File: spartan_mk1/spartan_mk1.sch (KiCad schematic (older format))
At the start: 0 parts

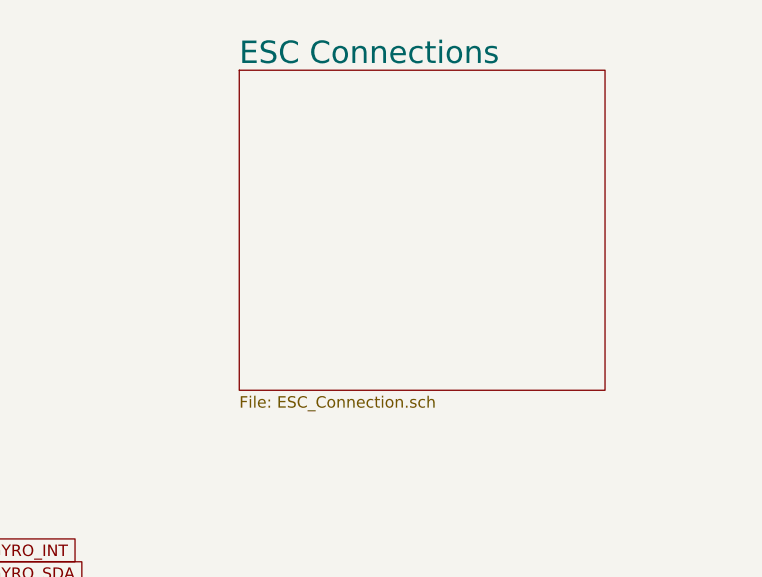
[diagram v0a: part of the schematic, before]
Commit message: Added ESC connectors in schematic
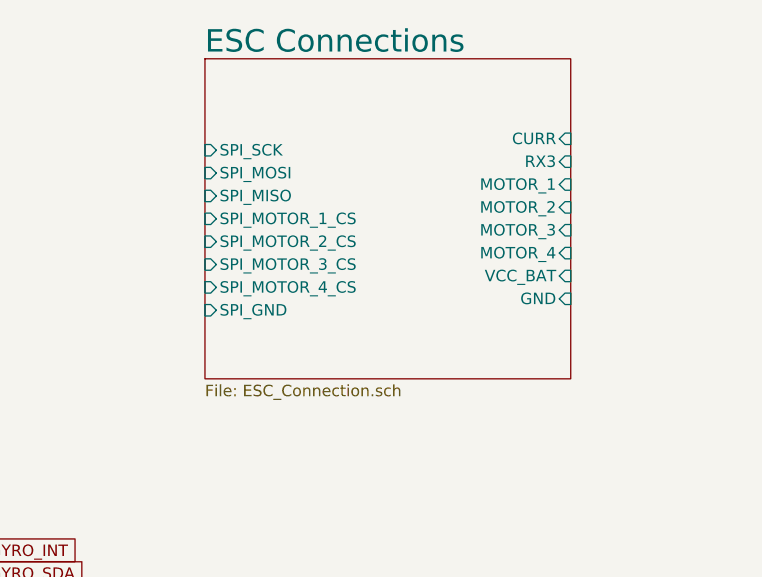
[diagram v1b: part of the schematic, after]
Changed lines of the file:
@@
 	7650 4150 7600 4150
 $Sheet
-S 8800 1450 1600 1400
+S 8650 1400 1600 1400
 U 5FB6E842
 F0 "ESC Connections" 98
 F1 "ESC_Connection.sch" 50
+F2 "GND" I R 10250 2450 50
+F3 "VCC_BAT" I R 10250 2350 50
+F4 "MOTOR_1" I R 10250 1950 50
+F5 "MOTOR_2" I R 10250 2050 50
+F6 "MOTOR_3" I R 10250 2150 50
+F7 "MOTOR_4" I R 10250 2250 50
+F8 "RX3" I R 10250 1850 50
+F9 "CURR" I R 10250 1750 50
+F10 "SPI_SCK" I L 8650 1800 50
+F11 "SPI_MOSI" I L 8650 1900 50
+F12 "SPI_MISO" I L 8650 2000 50
+F13 "SPI_MOTOR_1_CS" I L 8650 2100 50
+F14 "SPI_MOTOR_2_CS" I L 8650 2200 50
+F15 "SPI_MOTOR_3_CS" I L 8650 2300 50
+F16 "SPI_MOTOR_4_CS" I L 8650 2400 50
+F17 "SPI_GND" I L 8650 2500 50
 $EndSheet
 $Sheet

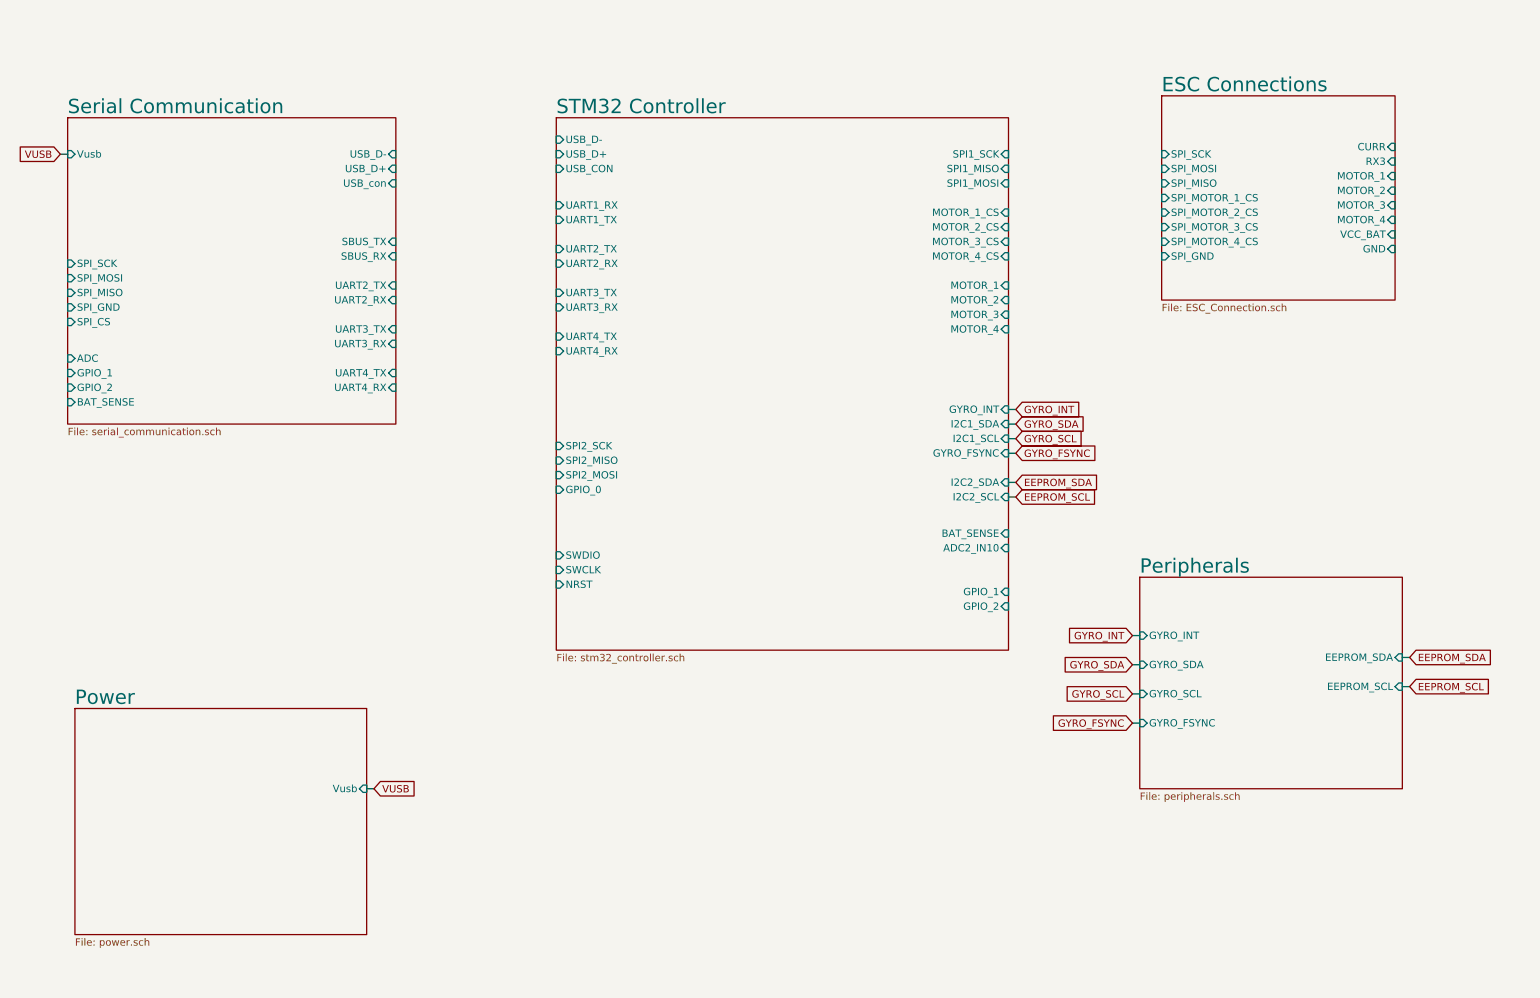
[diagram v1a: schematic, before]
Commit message: Complete schematic with DRC done
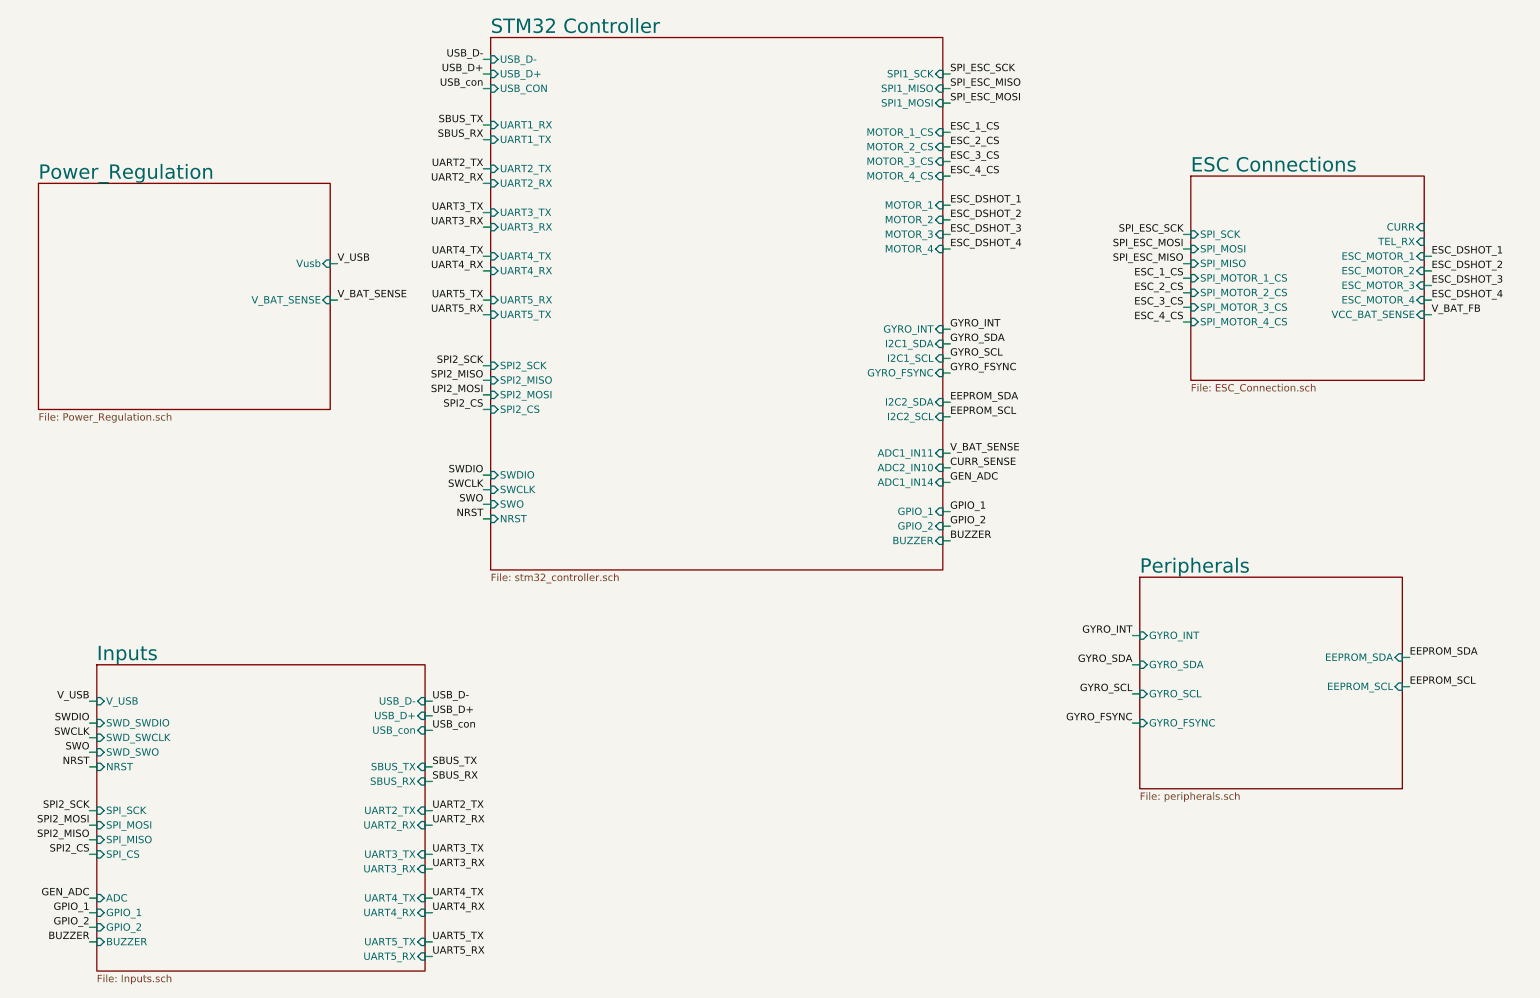
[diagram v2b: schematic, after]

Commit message: updated placement
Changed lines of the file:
@@
 Wire Wire Line
 	1300 5700 1350 5700
+Text Label 10500 2300 0    50   ~ 0
+CURR_SENSE
+Wire Wire Line
+	10500 2300 10450 2300
+Text Label 10500 2400 0    50   ~ 0
+UART3_RX
+Wire Wire Line
+	10500 2400 10450 2400
 $EndSCHEMATC

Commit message: Routing in progress
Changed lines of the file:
@@
 F7 "EEPROM_SCL" I R 10300 5450 50
 $EndSheet
-$Sheet
-S 1350 5300 2250 2100
-U 5F78701C
-F0 "Inputs" 98
-F1 "Inputs.sch" 50
-F2 "USB_D-" I R 3600 5550 50
-F3 "USB_D+" I R 3600 5650 50
-F4 "UART2_TX" I R 3600 6300 50
-F5 "UART2_RX" I R 3600 6400 50
-F6 "UART3_TX" I R 3600 6600 50
-F7 "UART3_RX" I R 3600 6700 50
-F8 "UART4_TX" I R 3600 6900 50
-F9 "UART4_RX" I R 3600 7000 50
-F10 "SPI_SCK" I L 1350 6300 50
-F11 "SPI_MOSI" I L 1350 6400 50
-F12 "SPI_MISO" I L 1350 6500 50
-F13 "SPI_CS" I L 1350 6600 50
-F14 "USB_con" I R 3600 5750 50
-F15 "GPIO_1" I L 1350 7000 50
-F16 "GPIO_2" I L 1350 7100 50
-F17 "ADC" I L 1350 6900 50
-F18 "SBUS_RX" I R 3600 6100 50
-F19 "SBUS_TX" I R 3600 6000 50
-F20 "UART5_TX" I R 3600 7200 50
-F21 "UART5_RX" I R 3600 7300 50
-F22 "V_USB" I L 1350 5550 50
-F23 "SWD_SWDIO" I L 1350 5700 50
-F24 "SWD_SWCLK" I L 1350 5800 50
-F25 "SWD_SWO" I L 1350 5900 50
-F26 "NRST" I L 1350 6000 50
-F27 "BUZZER" I L 1350 7200 50
-$EndSheet
 Wire Wire Line
 	8450 5100 8500 5100
@@
 Wire Wire Line
 	7200 3600 7150 3600
-$Sheet
-S 4050 1000 3100 3650
-U 5F6A010E
-F0 "STM32 Controller" 98
-F1 "stm32_controller.sch" 50
-F2 "USB_D-" I L 4050 1150 50
-F3 "USB_D+" I L 4050 1250 50
-F4 "UART1_RX" I L 4050 1600 50
-F5 "UART1_TX" I L 4050 1700 50
-F6 "UART2_TX" I L 4050 1900 50
-F7 "UART2_RX" I L 4050 2000 50
-F8 "UART3_TX" I L 4050 2200 50
-F9 "UART3_RX" I L 4050 2300 50
-F10 "UART4_TX" I L 4050 2500 50
-F11 "UART4_RX" I L 4050 2600 50
-F12 "I2C1_SDA" I R 7150 3100 50
-F13 "I2C1_SCL" I R 7150 3200 50
-F14 "I2C2_SCL" I R 7150 3600 50
-F15 "I2C2_SDA" I R 7150 3500 50
-F16 "SPI1_SCK" I R 7150 1250 50
-F17 "SPI1_MISO" I R 7150 1350 50
-F18 "SPI1_MOSI" I R 7150 1450 50
-F19 "SPI2_SCK" I L 4050 3250 50
-F20 "SPI2_MISO" I L 4050 3350 50
-F21 "SPI2_MOSI" I L 4050 3450 50
-F22 "MOTOR_4" I R 7150 2450 50
-F23 "MOTOR_3" I R 7150 2350 50
-F24 "MOTOR_2" I R 7150 2250 50
-F25 "MOTOR_1" I R 7150 2150 50
-F26 "GYRO_FSYNC" I R 7150 3300 50
-F27 "GYRO_INT" I R 7150 3000 50
-F28 "MOTOR_1_CS" I R 7150 1650 50
-F29 "MOTOR_2_CS" I R 7150 1750 50
-F30 "MOTOR_3_CS" I R 7150 1850 50
-F31 "MOTOR_4_CS" I R 7150 1950 50
-F32 "ADC2_IN10" I R 7150 3950 50
-F33 "GPIO_1" I R 7150 4250 50
-F34 "SWDIO" I L 4050 4000 50
-F35 "SWCLK" I L 4050 4100 50
-F36 "NRST" I L 4050 4300 50
-F37 "GPIO_2" I R 7150 4350 50
-F38 "USB_CON" I L 4050 1350 50
-F39 "UART5_RX" I L 4050 2800 50
-F40 "UART5_TX" I L 4050 2900 50
-F41 "SPI2_CS" I L 4050 3550 50
-F42 "ADC1_IN14" I R 7150 4050 50
-F43 "ADC1_IN11" I R 7150 3850 50
-F44 "SWO" I L 4050 4200 50
-F45 "BUZZER" I R 7150 4450 50
-$EndSheet
 Wire Wire Line
 	3000 2550 2950 2550
@@
 Wire Wire Line
 	3650 5650 3600 5650
-Text Label 3650 5750 0    50   ~ 0
-USB_con
-Wire Wire Line
-	3650 5750 3600 5750
 Text Label 4000 1150 2    50   ~ 0
 USB_D-
 Text Label 4000 1250 2    50   ~ 0
 USB_D+
-Text Label 4000 1350 2    50   ~ 0
-USB_con
-Wire Wire Line
-	4000 1350 4050 1350
 Wire Wire Line
 	4050 1250 4000 1250
@@
 F2 "Vusb" I R 2950 2550 50
 F3 "V_BAT_SENSE" I R 2950 2800 50
+F4 "ESC_BAT_SENSE" I R 2950 2900 50
 $EndSheet
 Text Label 1300 5550 2    50   ~ 0
@@
 Wire Wire Line
 	1300 5550 1350 5550
-Text Label 10500 2900 0    50   ~ 0
-V_BAT_FB
 Wire Wire Line
 	10500 2900 10450 2900
-Text Label 7200 3850 0    50   ~ 0
+Text Label 7200 4050 0    50   ~ 0
 V_BAT_SENSE
 Wire Wire Line
@@
 Wire Wire Line
 	7200 4350 7150 4350
-Text Label 1300 6300 2    50   ~ 0
-SPI2_SCK
-Wire Wire Line
-	1300 6300 1350 6300
-Text Label 1300 6400 2    50   ~ 0
-SPI2_MOSI
-Wire Wire Line
-	1300 6400 1350 6400
-Text Label 1300 6500 2    50   ~ 0
-SPI2_MISO
-Wire Wire Line
-	1300 6500 1350 6500
-Text Label 1300 6600 2    50   ~ 0
-SPI2_CS
-Text Label 4000 3250 2    50   ~ 0
-SPI2_SCK
-Text Label 4000 3450 2    50   ~ 0
-SPI2_MOSI
-Text Label 4000 3350 2    50   ~ 0
-SPI2_MISO
-Text Label 4000 3550 2    50   ~ 0
-SPI2_CS
-Wire Wire Line
-	1300 6600 1350 6600
-Wire Wire Line
-	4000 3250 4050 3250
-Wire Wire Line
-	4000 3350 4050 3350
-Wire Wire Line
-	4000 3450 4050 3450
-Wire Wire Line
-	4000 3550 4050 3550
 Text Label 3650 6000 0    50   ~ 0
 SBUS_TX
@@
 Wire Wire Line
 	3000 2800 2950 2800
-Text Label 7200 4050 0    50   ~ 0
+Text Label 7200 3850 0    50   ~ 0
 GEN_ADC
 Wire Wire Line
@@
 Wire Wire Line
 	10500 2400 10450 2400
+$Sheet
+S 1350 5300 2250 2100
+U 5F78701C
+F0 "Inputs" 98
+F1 "Inputs.sch" 50
+F2 "USB_D-" I R 3600 5550 50
+F3 "USB_D+" I R 3600 5650 50
+F4 "UART2_TX" I R 3600 6300 50
+F5 "UART2_RX" I R 3600 6400 50
+F6 "UART3_TX" I R 3600 6600 50
+F7 "UART3_RX" I R 3600 6700 50
+F8 "UART4_TX" I R 3600 6900 50
+F9 "UART4_RX" I R 3600 7000 50
+F10 "GPIO_1" I L 1350 7000 50
+F11 "GPIO_2" I L 1350 7100 50
+F12 "ADC" I L 1350 6900 50
+F13 "SBUS_RX" I R 3600 6100 50
+F14 "SBUS_TX" I R 3600 6000 50
+F15 "UART5_TX" I R 3600 7200 50
+F16 "UART5_RX" I R 3600 7300 50
+F17 "V_USB" I L 1350 5550 50
+F18 "SWD_SWDIO" I L 1350 5700 50
+F19 "SWD_SWCLK" I L 1350 5800 50
+F20 "SWD_SWO" I L 1350 5900 50
+F21 "NRST" I L 1350 6000 50
+F22 "BUZZER" I L 1350 7200 50
+$EndSheet
+$Sheet
+S 4050 1000 3100 3650
+U 5F6A010E
+F0 "STM32 Controller" 98
+F1 "stm32_controller.sch" 50
+F2 "USB_D-" I L 4050 1150 50
+F3 "USB_D+" I L 4050 1250 50
+F4 "UART1_RX" I L 4050 1600 50
+F5 "UART1_TX" I L 4050 1700 50
+F6 "UART2_TX" I L 4050 1900 50
+F7 "UART2_RX" I L 4050 2000 50
+F8 "UART3_TX" I L 4050 2200 50
+F9 "UART3_RX" I L 4050 2300 50
+F10 "UART4_TX" I L 4050 2500 50
+F11 "UART4_RX" I L 4050 2600 50
+F12 "I2C1_SDA" I R 7150 3100 50
+F13 "I2C1_SCL" I R 7150 3200 50
+F14 "I2C2_SCL" I R 7150 3600 50
+F15 "I2C2_SDA" I R 7150 3500 50
+F16 "SPI1_SCK" I R 7150 1250 50
+F17 "SPI1_MISO" I R 7150 1350 50
+F18 "SPI1_MOSI" I R 7150 1450 50
+F19 "MOTOR_4" I R 7150 2450 50
+F20 "MOTOR_3" I R 7150 2350 50
+F21 "MOTOR_2" I R 7150 2250 50
+F22 "MOTOR_1" I R 7150 2150 50
+F23 "GYRO_FSYNC" I R 7150 3300 50
+F24 "GYRO_INT" I R 7150 3000 50
+F25 "MOTOR_1_CS" I R 7150 1650 50
+F26 "MOTOR_2_CS" I R 7150 1750 50
+F27 "MOTOR_3_CS" I R 7150 1850 50
+F28 "MOTOR_4_CS" I R 7150 1950 50
+F29 "ADC2_IN10" I R 7150 3950 50
+F30 "GPIO_1" I R 7150 4250 50
+F31 "SWDIO" I L 4050 4000 50
+F32 "SWCLK" I L 4050 4100 50
+F33 "NRST" I L 4050 4300 50
+F34 "GPIO_2" I R 7150 4350 50
+F35 "UART5_RX" I L 4050 2800 50
+F36 "UART5_TX" I L 4050 2900 50
+F37 "ADC1_IN14" I R 7150 4050 50
+F38 "ADC1_IN11" I R 7150 3850 50
+F39 "SWO" I L 4050 4200 50
+F40 "BUZZER" I R 7150 4450 50
+$EndSheet
+Text Label 10500 2900 0    50   ~ 0
+ESC_BAT_SENSE
+Text Label 3000 2900 0    50   ~ 0
+ESC_BAT_SENSE
+Wire Wire Line
+	3000 2900 2950 2900
 $EndSCHEMATC
